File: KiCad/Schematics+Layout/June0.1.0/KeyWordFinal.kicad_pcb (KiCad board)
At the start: 2 copper layers, 54 parts, among them J1 USB4105-GF-A, J2 Conn_01x02_Pin, J3 Conn_01x05_Pin, J4 MSD-10-C, U1 NRF52805-CAAA-R, U2 NPM1100-CAAA-R7, U3 TXB0104RUTR, U4 TPS62743YFPR, U5 MCP6142T-E/MS, Y1 32.768k, Y3 32M

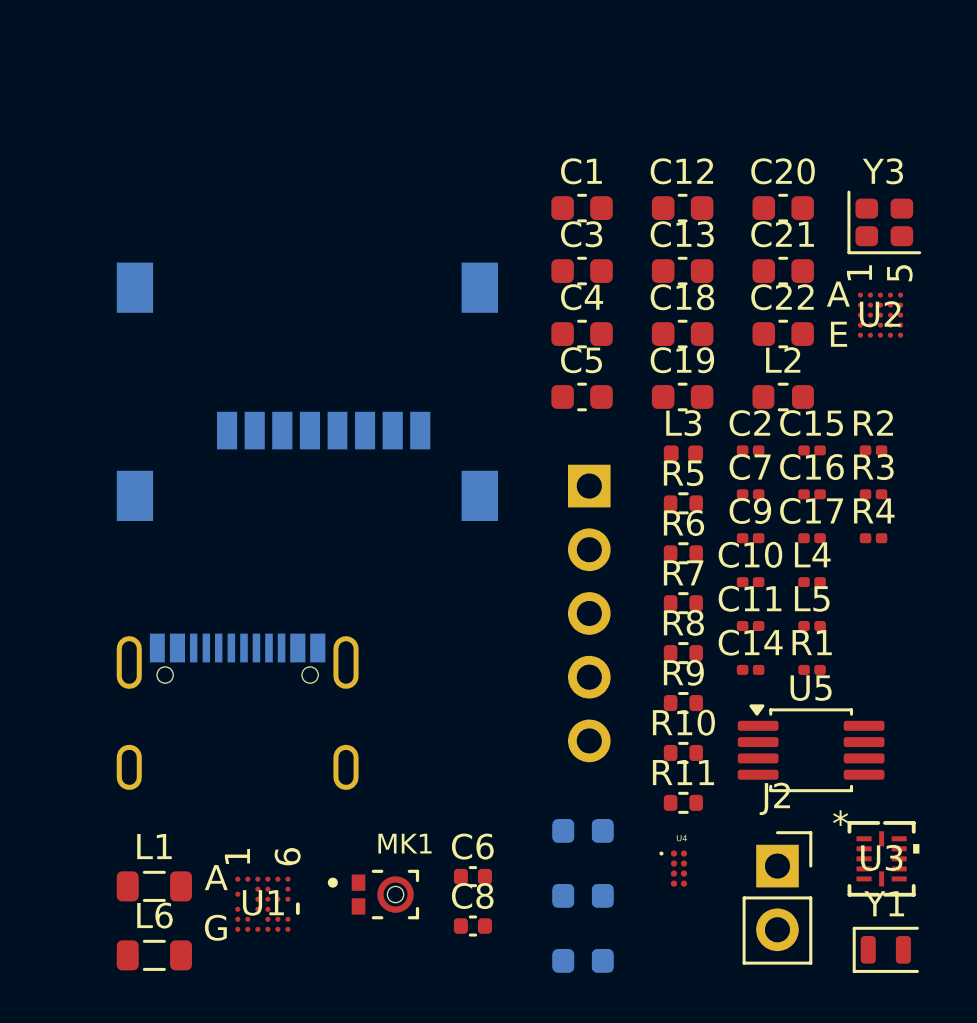
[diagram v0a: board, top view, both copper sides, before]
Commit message: Combine schematics and layout
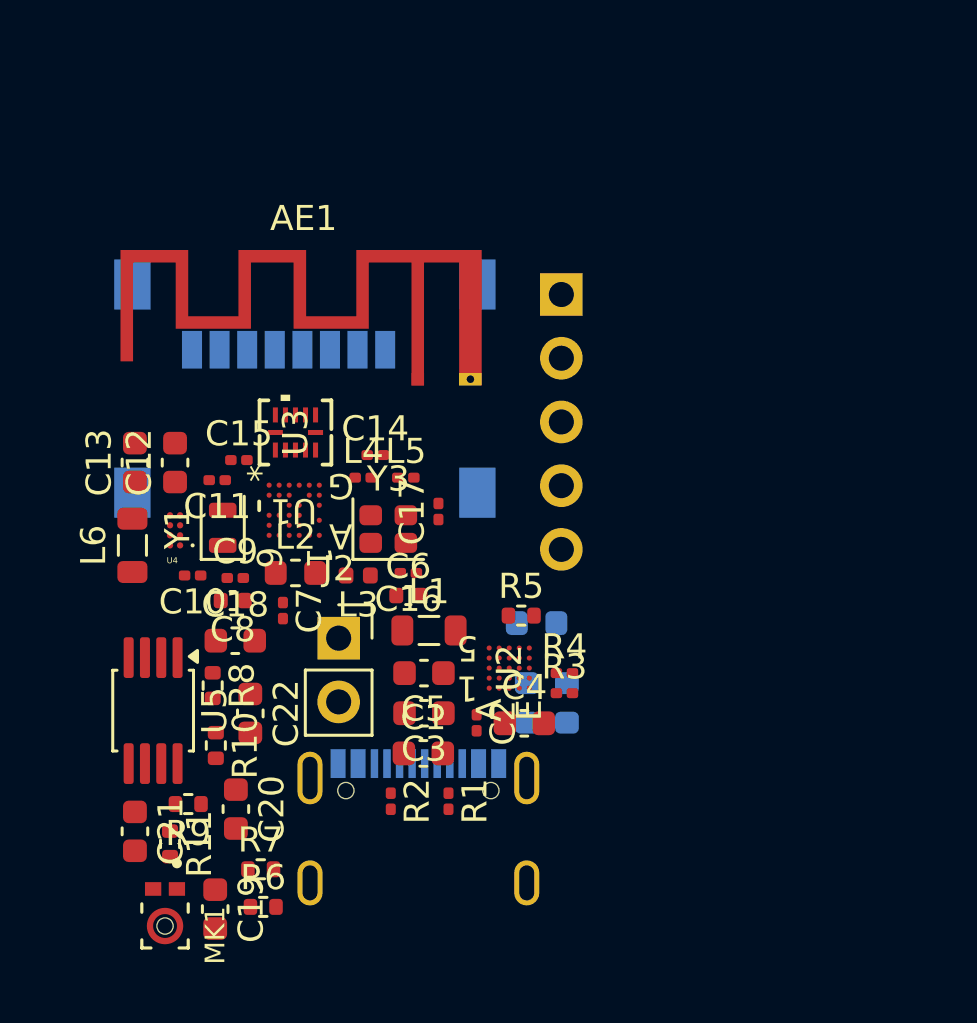
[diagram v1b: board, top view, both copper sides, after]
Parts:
- added AE1: Antenna_Chip, RF_Antenna:Texas_SWRA117D_2.4GHz_Left, F.Cu at (141.3, 59.1)
- moved C21 34.2 mm to (130.0, 77.1), turned to -90 degrees
- moved C20 32.4 mm to (134.0, 76.2), turned to -90 degrees
- moved Y1 31.3 mm to (133.5, 65.0), turned to 90 degrees
- moved U3 28.9 mm to (136.4, 61.2), turned to 90 degrees
- moved C19 27.6 mm to (133.2, 80.2), turned to -90 degrees
- moved U5 26.3 mm to (130.7, 72.3), turned to -90 degrees
- moved C22 26.1 mm to (134.6, 72.4), turned to -90 degrees
- moved U4 24.2 mm to (131.6, 65.1), turned to 180 degrees
- moved R2 23.8 mm to (140.2, 75.9), turned to -90 degrees
- moved Y3 23.2 mm to (140.1, 65.0)
- moved C13 23.1 mm to (130.0, 62.4), turned to 90 degrees
- moved C15 22.9 mm to (134.1, 62.3)
- moved C1 22.6 mm to (141.5, 74.0)
- moved C12 22.6 mm to (131.6, 62.4), turned to 90 degrees
- moved C10 22.2 mm to (132.3, 66.9), turned to 180 degrees
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
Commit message: Updated layout, updated schematic to ease layout.
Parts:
- added C23: 0.1u, Capacitor_SMD:C_0603_1608Metric, F.Cu at (133.2, 73.7)
- added C24: 0.1u, Capacitor_SMD:C_0603_1608Metric, F.Cu at (131.6, 77.4)
- added C25: 0.1u, Capacitor_SMD:C_0603_1608Metric, F.Cu at (134.0, 59.5)
- added C26: 0.1u, Capacitor_SMD:C_0603_1608Metric, F.Cu at (134.5, 57.8)
- added C27: 1.0u, Capacitor_SMD:C_0603_1608Metric, F.Cu at (134.5, 56.3)
- added C28: 0.1u, Capacitor_SMD:C_0603_1608Metric, F.Cu at (136.7, 57.0)
- C19: value C -> 10n
- R6, R7: value R -> 100k
- moved D3 18.7 mm to (146.2, 50.1), turned to 180 degrees
- moved R5 18.7 mm to (148.4, 50.1)
- moved J3 17.3 mm to (130.8, 49.9), turned to -90 degrees
- moved J2 12.0 mm to (148.5, 75.4)
- moved U4 8.13 mm to (130.8, 57.0)
- moved L6 6.39 mm to (130.6, 59.3), turned to 0 degrees
- moved C17 6.29 mm to (138.4, 69.5), turned to 180 degrees
- moved AE1 6.21 mm to (144.9, 64.1), turned to -90 degrees
- moved C12 5.92 mm to (129.4, 56.9)
- moved C13 5.89 mm to (132.3, 57.0)
- moved C5 5.42 mm to (146.4, 68.5), turned to 0 degrees
- moved C6 5.20 mm to (135.7, 67.0), turned to 90 degrees
- moved C2 4.69 mm to (148.3, 72.7)
- moved L3 4.21 mm to (135.1, 68.6)
- moved Y3 3.43 mm to (138.5, 68.1)
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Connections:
- U1 pad F2: Net-(U1-P0.20) -> Net-(D3-A)
- U1 pad F4: Net-(D3-A) -> Net-(U1-P0.14)
- U1 pad F5: VCOM -> /ADC+
- U1 pad F6: /ADC+ -> VCOM
- U3 pad 11: Net-(J4-CLK) -> +3V0
- U3 pad 12: Net-(J4-CMD) -> +1V8
- U3 pad 2: Net-(U1-P0.20) -> Net-(U1-P0.12)
- U3 pad 3: Net-(U1-P0.18) -> Net-(U1-P0.16)
- U3 pad 4: Net-(U1-P0.16) -> Net-(U1-P0.18)
- U3 pad 5: Net-(U1-P0.12) -> Net-(U1-P0.14)
- U3 pad 6: unconnected-(U3-NC-Pad6) -> GND
- U3 pad 7: GND -> Net-(J4-DAT3/CD)
- U3 pad 8: +1V8 -> Net-(J4-CMD)
- U3 pad 9: unconnected-(U3-NC-Pad9) -> Net-(J4-CLK)
- Y3 pad 1: Net-(U1-XC1) -> Net-(U1-XC2)
- Y3 pad 3: Net-(U1-XC2) -> Net-(U1-XC1)
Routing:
- net Net-(D3-A): track 0.00 -> 19.9 mm, vias 0 -> 3
- net Net-(J3-Pin_3): track 0.00 -> 17.0 mm
- net Net-(J3-Pin_5): track 0.00 -> 15.3 mm
- net Net-(J3-Pin_4): track 0.00 -> 15.1 mm
- net /ADC+: track 0.00 -> 14.7 mm
- net VCOM: track 0.00 -> 14.6 mm
- net GND: track 0.00 -> 8.12 mm, vias 0 -> 102
- net Net-(U1-DEC2): track 0.00 -> 5.43 mm
- net /RF: track 0.00 -> 5.21 mm
- net Net-(U1-XC2): track 0.00 -> 5.16 mm
- net Net-(U1-P0.01/XL2): track 0.00 -> 4.74 mm
- net Net-(U1-P0.14): track 0.00 -> 4.39 mm, vias 0 -> 2
- net Net-(U1-XC1): track 0.00 -> 3.96 mm
- net Net-(U1-P0.00/XL1): track 0.00 -> 3.35 mm
- net Net-(U1-P0.12): track 0.00 -> 2.84 mm
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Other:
- board outline added: 21.6 x 33.9 mm
- rule pad_to_mask_clearance: 0 -> 0.0762

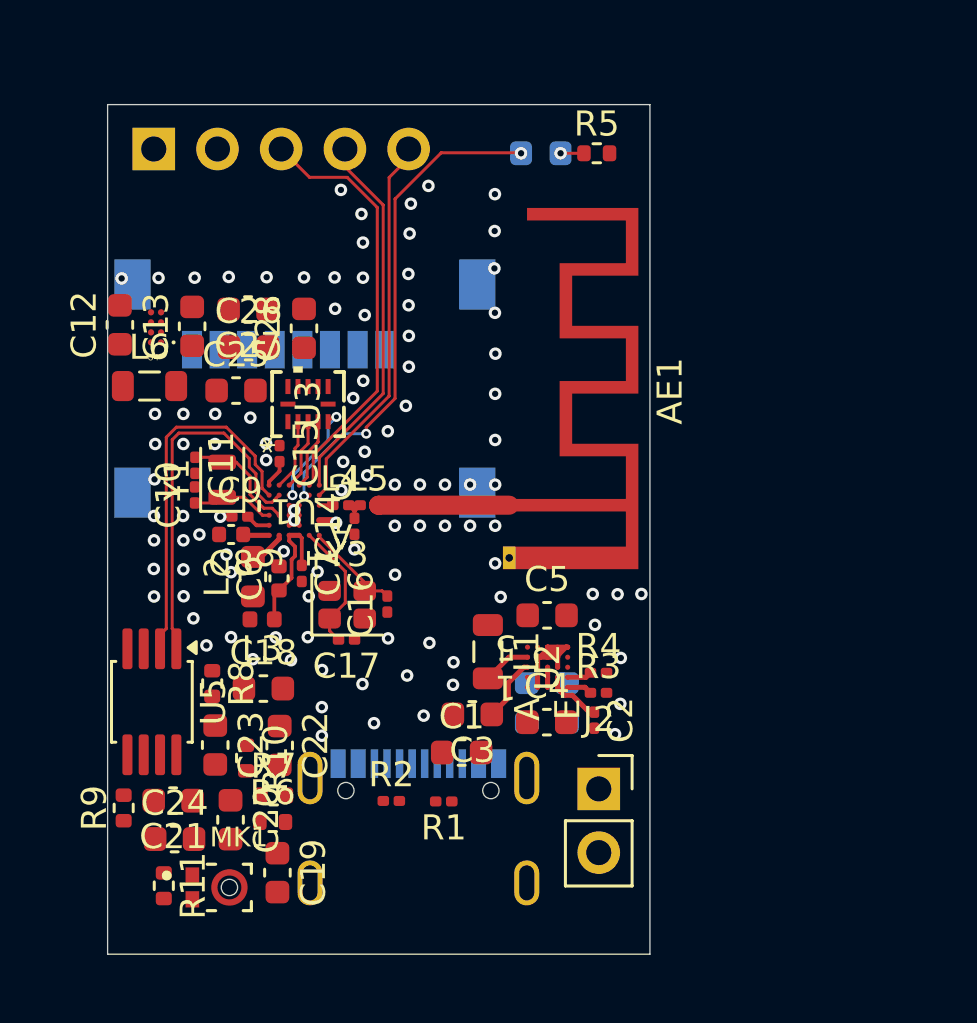
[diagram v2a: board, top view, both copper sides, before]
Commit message: Added some traces to test placement
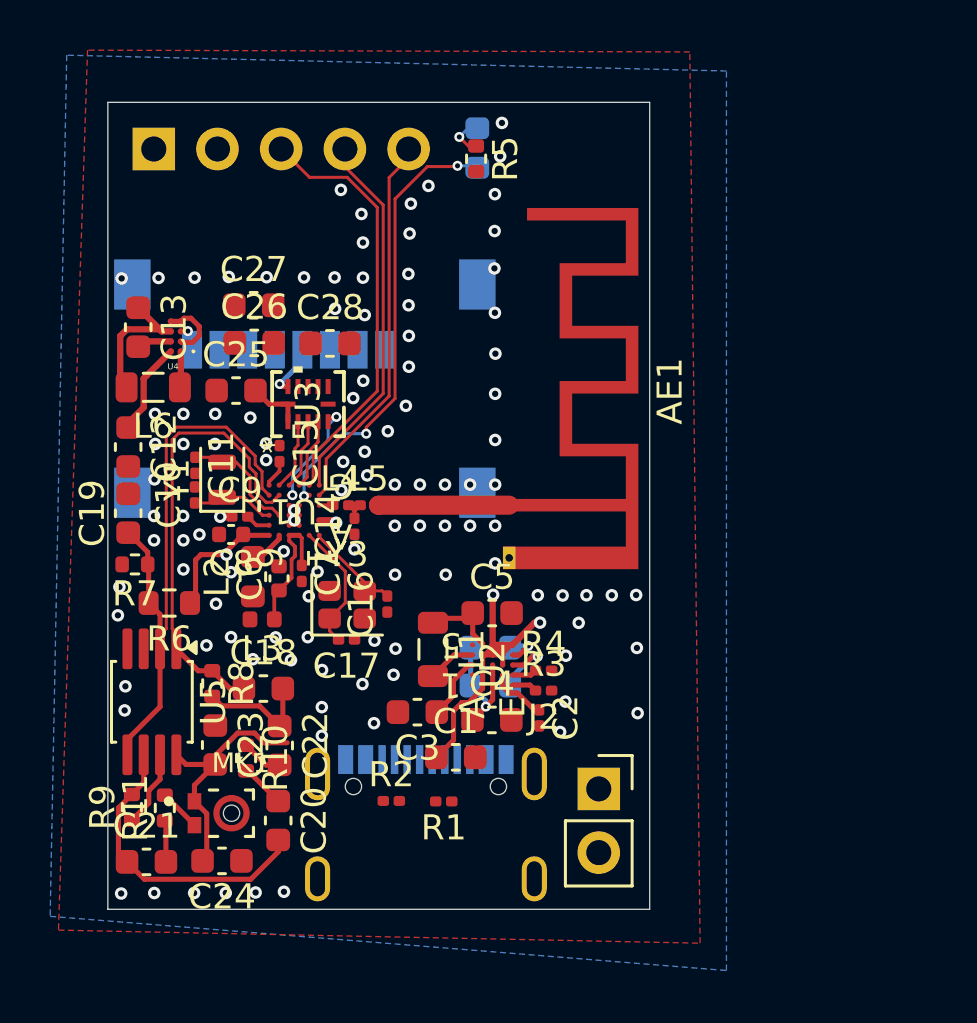
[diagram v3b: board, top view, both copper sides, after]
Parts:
- R6: footprint Resistor_SMD:R_0402_1005Metric -> Resistor_SMD:R_0603_1608Metric
- moved C19 15.5 mm to (129.7, 64.4), turned to 90 degrees
- moved R7 10.7 mm to (130.0, 66.5), turned to 180 degrees
- moved R6 9.65 mm to (131.4, 68.0), turned to 180 degrees
- moved C12 4.88 mm to (129.7, 61.8), turned to -90 degrees
- moved R5 4.82 mm to (143.6, 50.3), turned to -90 degrees
- moved D2 3.76 mm to (144.2, 69.8), turned to 180 degrees
- moved R11 3.10 mm to (131.2, 76.2), turned to 90 degrees
- moved MK1 2.96 mm to (133.4, 76.4)
- moved C21 2.66 mm to (130.5, 78.3), turned to 0 degrees
- moved D3 2.54 mm to (143.7, 49.9), turned to -90 degrees
- moved C2 2.19 mm to (146.1, 72.6)
- moved C5 2.19 mm to (144.2, 68.4)
- moved R4 2.19 mm to (146.3, 70.7)
- moved U2 2.19 mm to (144.3, 70.5)
- moved C3 2.19 mm to (141.3, 72.3)
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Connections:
- C12 pad 1: V_{INT} -> VBUS
- U4 pad A2: V_{INT} -> VBUS
- U4 pad B1: V_{INT} -> VBUS
- U4 pad D1: V_{INT} -> VBUS
- U4 pad D2: V_{INT} -> VBUS
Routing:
- net +1V8: track 2.16 -> 21.7 mm, vias 0 -> 1
- net Net-(C20-Pad2): track 0.00 -> 12.1 mm
- net VBUS: track 0.40 -> 10.5 mm
- net VCOM: track 14.6 -> 24.5 mm
- net +3V0: track 0.00 -> 7.64 mm, vias 0 -> 1
- net GND: track 8.12 -> 14.1 mm, vias 102 -> 114
- net Net-(C20-Pad1): track 0.00 -> 4.84 mm
- net Net-(C18-Pad2): track 0.00 -> 4.73 mm
- net V_{INT}: track 0.80 -> 5.12 mm, vias 0 -> 1
- net /ADC+: track 14.7 -> 18.0 mm
- net Net-(D1-K): track 0.00 -> 2.87 mm, vias 0 -> 1
- net Net-(D3-A): track 19.9 -> 18.0 mm
- net /Mic: track 0.00 -> 1.68 mm
- net Net-(C22-Pad2): track 0.00 -> 1.67 mm
- net Net-(C21-Pad2): track 0.00 -> 1.66 mm
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- added copper zone on B.Cu, net GND
- added copper zone on F.Cu, net GND
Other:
- board size 21.6 x 33.9 mm -> 21.6 x 32.2 mm
